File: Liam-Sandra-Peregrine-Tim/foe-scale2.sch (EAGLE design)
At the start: 52 parts, among them U1 LM311, U2 SAMD21E

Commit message: fixed up a couple things in board
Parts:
- added R18: 0, resistor:R-US_R0805
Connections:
- net AGND: now also R18.2
- net DGND: now also R18.1
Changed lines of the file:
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@@
 <?xml version="1.0" encoding="utf-8"?>
 <!DOCTYPE eagle SYSTEM "eagle.dtd">
-<eagle version="7.5.0">
+<eagle version="7.4.0">
 <drawing>
 <settings>
@@
 <part name="U$4" library="foe-scale" deviceset="TEST_POINT" device=""/>
 <part name="U$5" library="foe-scale" deviceset="TEST_POINT" device=""/>
+<part name="R18" library="resistor" deviceset="R-US_" device="R0805" value="0"/>
+<part name="SUPPLY31" library="supply2" deviceset="AGND" device=""/>
+<part name="SUPPLY32" library="supply2" deviceset="DGND" device=""/>
 </parts>
 <sheets>
@@
 <instance part="U$4" gate="G$1" x="68.58" y="-129.54" rot="R180"/>
 <instance part="U$5" gate="G$1" x="68.58" y="-139.7" rot="R180"/>
+<instance part="R18" gate="G$1" x="325.12" y="-76.2" rot="R180"/>
+<instance part="SUPPLY31" gate="G$1" x="312.42" y="-81.28"/>
+<instance part="SUPPLY32" gate="G$1" x="337.82" y="-81.28"/>
 </instances>
 <busses>
@@
 <wire x1="337.82" y1="-58.42" x2="337.82" y2="-60.96" width="0.1524" layer="91"/>
 </segment>
+<segment>
+<pinref part="R18" gate="G$1" pin="1"/>
+<wire x1="330.2" y1="-76.2" x2="337.82" y2="-76.2" width="0.1524" layer="91"/>
+<wire x1="337.82" y1="-76.2" x2="337.82" y2="-78.74" width="0.1524" layer="91"/>
+<pinref part="SUPPLY32" gate="G$1" pin="DGND"/>
+</segment>
 </net>
 <net name="DO-PA16" class="0">
@@
 <wire x1="312.42" y1="-58.42" x2="320.04" y2="-58.42" width="0.1524" layer="91"/>
 </segment>
-</net>
+<segment>
+<pinref part="R18" gate="G$1" pin="2"/>
+<wire x1="320.04" y1="-76.2" x2="312.42" y2="-76.2" width="0.1524" layer="91"/>
+<wire x1="312.42" y1="-76.2" x2="312.42" y2="-78.74" width="0.1524" layer="91"/>
+<pinref part="SUPPLY31" gate="G$1" pin="AGND"/>
+</segment>
+</net>

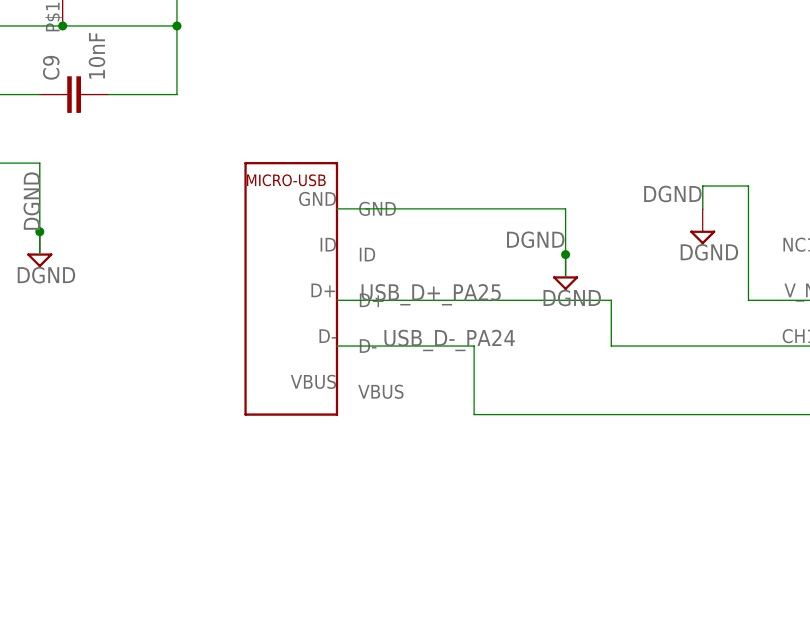
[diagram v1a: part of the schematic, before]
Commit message: replaced microUSB with standard USB B
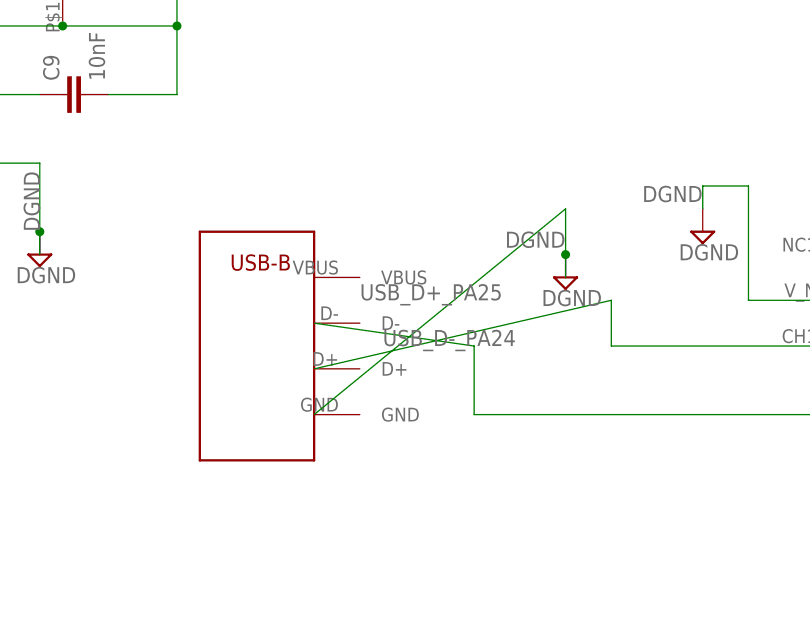
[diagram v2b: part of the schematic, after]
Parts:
- U$13: value MICRO-USB-CONNECTOR -> USB-B; device foe-scale:MICRO-USB-CONNECTOR -> foe-scale:USB-B
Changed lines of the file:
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@@
 <?xml version="1.0" encoding="utf-8"?>
 <!DOCTYPE eagle SYSTEM "eagle.dtd">
-<eagle version="7.4.0">
+<eagle version="7.5.0">
 <drawing>
 <settings>
@@
 <part name="C7" library="rcl" deviceset="C-EU" device="C0805K" value="100nF"/>
 <part name="U$10" library="foe-scale" deviceset="RGBLED" device=""/>
-<part name="U$13" library="foe-scale" deviceset="MICRO-USB-CONNECTOR" device=""/>
+<part name="U$13" library="foe-scale" deviceset="USB-B" device=""/>
 <part name="AS1363" library="foe-scale" deviceset="3.3V_AS1363" device=""/>
 <part name="R11" library="resistor" deviceset="R-US_" device="R0805" value="10k"/>
@@
 <segment>
 <pinref part="U$13" gate="G$1" pin="GND"/>
-<wire x1="215.9" y1="-7.62" x2="241.3" y2="-7.62" width="0.1524" layer="91"/>
+<wire x1="213.36" y1="-30.48" x2="241.3" y2="-7.62" width="0.1524" layer="91"/>
 <wire x1="241.3" y1="-7.62" x2="241.3" y2="-12.7" width="0.1524" layer="91"/>
 <label x="241.3" y="-10.16" size="1.778" layer="95" rot="R180"/>
@@
 <segment>
 <pinref part="U$13" gate="G$1" pin="D-"/>
-<wire x1="215.9" y1="-22.86" x2="231.14" y2="-22.86" width="0.1524" layer="91"/>
+<wire x1="213.36" y1="-20.32" x2="231.14" y2="-22.86" width="0.1524" layer="91"/>
 <wire x1="231.14" y1="-22.86" x2="231.14" y2="-30.48" width="0.1524" layer="91"/>
 <wire x1="231.14" y1="-30.48" x2="289.56" y2="-30.48" width="0.1524" layer="91"/>
@@
 <segment>
 <pinref part="U$13" gate="G$1" pin="D+"/>
-<wire x1="215.9" y1="-17.78" x2="246.38" y2="-17.78" width="0.1524" layer="91"/>
+<wire x1="213.36" y1="-25.4" x2="246.38" y2="-17.78" width="0.1524" layer="91"/>
 <wire x1="246.38" y1="-17.78" x2="246.38" y2="-22.86" width="0.1524" layer="91"/>
 <pinref part="D1" gate="G$1" pin="CH1"/>
